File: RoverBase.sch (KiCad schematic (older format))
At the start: 62 parts, among them J1 Conn_01x01, J2 Conn_01x06, J3 Conn_01x04, J4 Conn_01x02, J5 Conn_01x03, J6 Conn_02x03_Counter_Clockwise, J7 Conn_02x03_Counter_Clockwise, J8 Conn_01x01, J9 Conn_01x06, SW1 SW_SPDT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

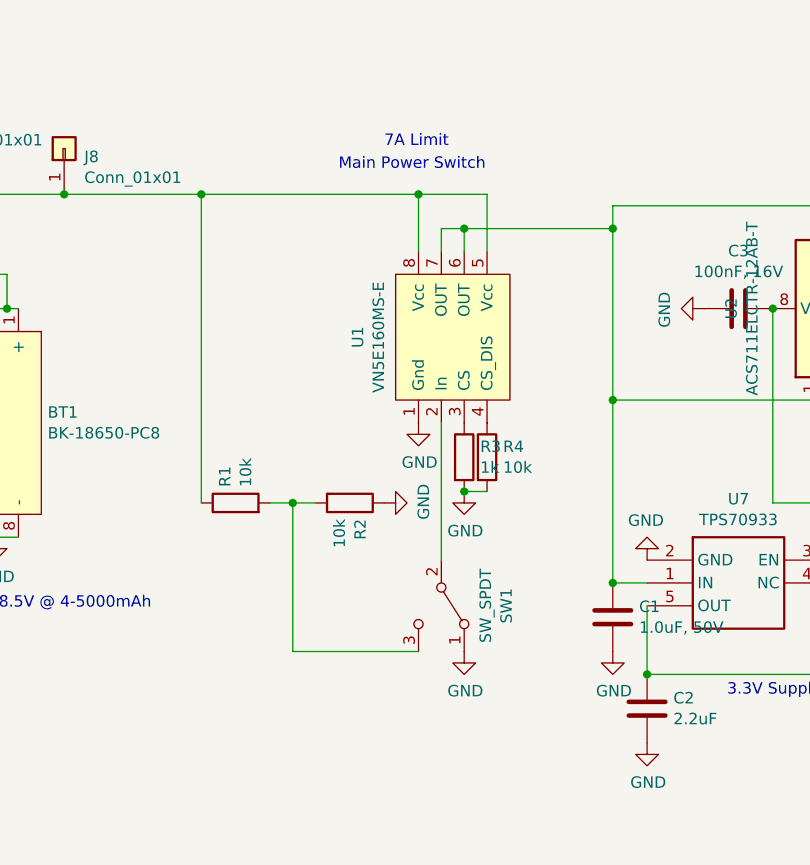
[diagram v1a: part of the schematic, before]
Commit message: Using FET and fuse instead of switch
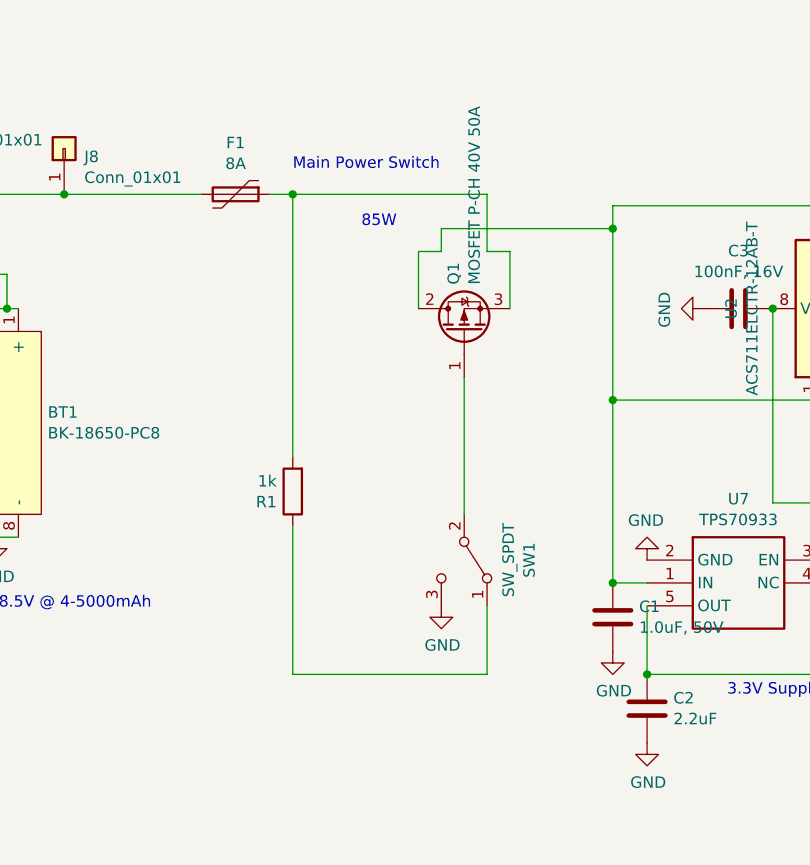
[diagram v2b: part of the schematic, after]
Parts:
- removed R2, R4: 10k, Resistor_SMD:R_0402_1005Metric_Pad0.72x0.64mm_HandSolder, symbol Device:R
- removed R3: 1k, Resistor_SMD:R_0402_1005Metric_Pad0.72x0.64mm_HandSolder, symbol Device:R
- removed U1: VN5E160MS-E, Package_SO:SO-8_3.9x4.9mm_P1.27mm, symbol ST_Switch:VN5E160MS-E
- added F1: 8A, Fuse:Fuse_Bourns_MF-RG800, symbol Device:Polyfuse
- added Q1: MOSFET P-CH 40V 50A, Package_TO_SOT_SMD:TO-263-2, symbol Device:Q_PMOS_GDS
- R1: value 10k -> 1k; MPN CRCW040210K0FKED -> CRCW04021K00FKEDHP; SPN 541-3959-1-ND -> 541-1.00KYCT-ND
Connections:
- net GND: now also SW1.3 (C); no longer SW1.1 (A)
- net at C1.1, R5.1, U2.1 (IP+)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: now also Q1.2 (D)
- net at SW1.2 (B): now also Q1.1 (G)
- net at BT1.3 (+), BT1.4 (+), J8.1 (Pin_1): now also F1.2; no longer R1.1
- net at R1.2: now also F1.1, Q1.3 (S); no longer SW1.3 (C)
- new net: R1.1, SW1.1 (A)
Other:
- note added: "85W"
- note removed: "7A Limit"
- moved on the sheet: SW1
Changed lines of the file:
@@
 Wire Wire Line
 	8450 1750 8350 1750
-Text Notes 3300 1200 0    50   ~ 0
+Text Notes 3100 1200 0    50   ~ 0
 Main Power Switch
 $Comp
@@
 Wire Wire Line
 	4500 1350 4500 1450
-Wire Wire Line
-	3950 1300 3650 1300
-Connection ~ 3650 1300
-Wire Wire Line
-	3650 1300 2700 1300
-Wire Wire Line
-	3750 1450 3850 1450
 Connection ~ 4500 1450
 Wire Wire Line
 	4500 1450 4500 2200
-Connection ~ 3850 1450
 Wire Wire Line
 	3950 1550 3950 1300
 Wire Wire Line
-	3850 1550 3850 1450
-Wire Wire Line
 	3750 1550 3750 1450
-Wire Wire Line
-	3650 1550 3650 1300
-$Comp
-L ST_Switch:VN5E160MS-E U1
-U 1 1 5FB454D3
-P 3550 1950
-F 0 "U1" H 3575 2115 50  0000 C CNN
-F 1 "VN5E160MS-E" H 3575 2024 50  0000 C CNN
-F 2 "Package_SO:SO-8_3.9x4.9mm_P1.27mm" H 3350 1400 50  0001 C CNN
-F 3 "https://www.st.com/content/ccc/resource/technical/document/datasheet/group2/73/be/a4/20/c7/b9/4c/b0/CD00235846/files/CD00235846.pdf/jcr:content/translations/en.CD00235846.pdf" H 3350 1400 50  0001 C CNN
-F 4 "497-11685-1-ND" H 3550 1950 50  0001 C CNN "SPN"
-F 5 "VN5E160MSTR-E" H 3550 1950 50  0001 C CNN "MPN"
-F 6 "STMicroelectronics" H 3550 1950 50  0001 C CNN "Manufacturer"
-	1    3550 1950
-	0    -1   -1   0
-$EndComp
 Text Notes 1150 2500 1    50   ~ 0
 4A max discharge
 $Comp
-L power:GND #PWR04
-U 1 1 5FB52F4F
-P 3650 2300
-F 0 "#PWR04" H 3650 2050 50  0001 C CNN
-F 1 "GND" H 3655 2127 50  0000 C CNN
-F 2 "" H 3650 2300 50  0001 C CNN
-F 3 "" H 3650 2300 50  0001 C CNN
-	1    3650 2300
-	1    0    0    -1
-$EndComp
-$Comp
-L Device:R R3
-U 1 1 5FB5349F
-P 3850 2450
-F 0 "R3" H 3920 2496 50  0000 L CNN
-F 1 "1k" H 3920 2405 50  0000 L CNN
-F 2 "Resistor_SMD:R_0402_1005Metric_Pad0.72x0.64mm_HandSolder" V 3780 2450 50  0001 C CNN
-F 3 "~" H 3850 2450 50  0001 C CNN
-F 4 "CRCW04021K00FKEDHP" H 3850 2450 50  0001 C CNN "MPN"
-F 5 "541-1.00KYCT-ND" H 3850 2450 50  0001 C CNN "SPN"
-F 6 "Vishay Dale" H 3850 2450 50  0001 C CNN "Manufacturer"
-	1    3850 2450
-	1    0    0    -1
-$EndComp
-$Comp
-L Device:R R4
-U 1 1 5FB53A58
-P 3950 2450
-F 0 "R4" H 4020 2496 50  0000 L CNN
-F 1 "10k" H 4020 2405 50  0000 L CNN
-F 2 "Resistor_SMD:R_0402_1005Metric_Pad0.72x0.64mm_HandSolder" V 3880 2450 50  0001 C CNN
-F 3 "~" H 3950 2450 50  0001 C CNN
-F 4 "CRCW040210K0FKED" H 3950 2450 50  0001 C CNN "MPN"
-F 5 "541-3959-1-ND" H 3950 2450 50  0001 C CNN "SPN"
-F 6 "Vishay Dale" H 3950 2450 50  0001 C CNN "Manufacturer"
-	1    3950 2450
-	1    0    0    -1
-$EndComp
-$Comp
-L Device:R R1
-U 1 1 5FB5423C
-P 2850 2650
-F 0 "R1" H 2920 2696 50  0000 L CNN
-F 1 "10k" H 2920 2605 50  0000 L CNN
-F 2 "Resistor_SMD:R_0402_1005Metric_Pad0.72x0.64mm_HandSolder" V 2780 2650 50  0001 C CNN
-F 3 "~" H 2850 2650 50  0001 C CNN
-F 4 "CRCW040210K0FKED" H 2850 2650 50  0001 C CNN "MPN"
-F 5 "541-3959-1-ND" H 2850 2650 50  0001 C CNN "SPN"
-F 6 "Vishay Dale" H 2850 2650 50  0001 C CNN "Manufacturer"
-	1    2850 2650
-	0    -1   -1   0
-$EndComp
-$Comp
-L Device:R R2
-U 1 1 5FB547F5
-P 3350 2650
-F 0 "R2" H 3420 2696 50  0000 L CNN
-F 1 "10k" H 3420 2605 50  0000 L CNN
-F 2 "Resistor_SMD:R_0402_1005Metric_Pad0.72x0.64mm_HandSolder" V 3280 2650 50  0001 C CNN
-F 3 "~" H 3350 2650 50  0001 C CNN
-F 4 "CRCW040210K0FKED" H 3350 2650 50  0001 C CNN "MPN"
-F 5 "541-3959-1-ND" H 3350 2650 50  0001 C CNN "SPN"
-F 6 "Vishay Dale" H 3350 2650 50  0001 C CNN "Manufacturer"
-	1    3350 2650
-	0    1    1    0
-$EndComp
-Wire Wire Line
-	2700 2650 2700 1300
-Connection ~ 2700 1300
-Wire Wire Line
-	3950 2600 3850 2600
-$Comp
-L power:GND #PWR05
-U 1 1 5FB578B0
-P 3850 2600
-F 0 "#PWR05" H 3850 2350 50  0001 C CNN
-F 1 "GND" H 3855 2427 50  0000 C CNN
-F 2 "" H 3850 2600 50  0001 C CNN
-F 3 "" H 3850 2600 50  0001 C CNN
-	1    3850 2600
-	1    0    0    -1
-$EndComp
-Connection ~ 3850 2600
-$Comp
-L power:GND #PWR03
-U 1 1 5FB57DBB
-P 3500 2650
-F 0 "#PWR03" H 3500 2400 50  0001 C CNN
-F 1 "GND" H 3505 2477 50  0000 C CNN
-F 2 "" H 3500 2650 50  0001 C CNN
-F 3 "" H 3500 2650 50  0001 C CNN
-	1    3500 2650
-	0    -1   -1   0
-$EndComp
-$Comp
 L Switch:SW_SPDT SW1
 U 1 1 5FB5A453
-P 3750 3100
-F 0 "SW1" H 3750 3385 50  0000 C CNN
-F 1 "SW_SPDT" H 3750 3294 50  0000 C CNN
-F 2 "Button_Switch_THT:SW_CuK_OS102011MA1QN1_SPDT_Angled" H 3750 3100 50  0001 C CNN
-F 3 "~" H 3750 3100 50  0001 C CNN
-F 4 "OS102011MA1QN1" H 3750 3100 50  0001 C CNN "MPN"
-F 5 "CKN9559-ND" H 3750 3100 50  0001 C CNN "SPN"
-F 6 "C&K" H 3750 3100 50  0001 C CNN "Manufacturer"
-	1    3750 3100
+P 3850 2900
+F 0 "SW1" H 3850 3185 50  0000 C CNN
+F 1 "SW_SPDT" H 3850 3094 50  0000 C CNN
+F 2 "Button_Switch_THT:SW_CuK_OS102011MA1QN1_SPDT_Angled" H 3850 2900 50  0001 C CNN
+F 3 "~" H 3850 2900 50  0001 C CNN
+F 4 "OS102011MA1QN1" H 3850 2900 50  0001 C CNN "MPN"
+F 5 "CKN9559-ND" H 3850 2900 50  0001 C CNN "SPN"
+F 6 "C&K" H 3850 2900 50  0001 C CNN "Manufacturer"
+	1    3850 2900
 	0    1    1    0
 $EndComp
-Wire Wire Line
-	3750 2300 3750 2900
-Wire Wire Line
-	3650 3300 3100 3300
-Wire Wire Line
-	3100 3300 3100 2650
-Wire Wire Line
-	3100 2650 3000 2650
-Wire Wire Line
-	3200 2650 3100 2650
-Connection ~ 3100 2650
 $Comp
 L power:GND #PWR06
 U 1 1 5FB65CD7
-P 3850 3300
-F 0 "#PWR06" H 3850 3050 50  0001 C CNN
-F 1 "GND" H 3855 3127 50  0000 C CNN
-F 2 "" H 3850 3300 50  0001 C CNN
-F 3 "" H 3850 3300 50  0001 C CNN
-	1    3850 3300
+P 3750 3100
+F 0 "#PWR06" H 3750 2850 50  0001 C CNN
+F 1 "GND" H 3755 2927 50  0000 C CNN
+F 2 "" H 3750 3100 50  0001 C CNN
+F 3 "" H 3750 3100 50  0001 C CNN
+	1    3750 3100
 	1    0    0    -1
 $EndComp
@@
 	0    1    1    0
 $EndComp
-Text Notes 3500 1100 0    50   ~ 0
-7A Limit
+Text Notes 3400 1450 0    50   ~ 0
+85W
 Wire Wire Line
 	7100 4900 7200 4900
@@
 $EndComp
 Wire Wire Line
-	3850 1450 4500 1450
-Wire Wire Line
 	7200 4900 8200 4900
 $Comp
@@
 Connection ~ 2100 1300
 Wire Wire Line
-	2100 1300 2700 1300
-Wire Wire Line
 	1450 1300 2100 1300
 $Comp
@@
 	9350 4900 9050 4900
 Connection ~ 9350 4900
+$Comp
+L Device:Q_PMOS_GDS Q1
+U 1 1 60C92188
+P 3850 1900
+F 0 "Q1" H 4055 1946 50  0000 L CNN
+F 1 " MOSFET P-CH 40V 50A" H 4055 1855 50  0000 L CNN
+F 2 "Package_TO_SOT_SMD:TO-263-2" H 4050 2000 50  0001 C CNN
+F 3 "~" H 3850 1900 50  0001 C CNN
+F 4 "SQM40081EL_GE3" H 3850 1900 50  0001 C CNN "MPN"
+F 5 "Vishay Siliconix" H 3850 1900 50  0001 C CNN "Manufacturer"
+F 6 "SQM40081EL_GE3CT-ND" H 3850 1900 50  0001 C CNN "SPN"
+	1    3850 1900
+	0    -1   -1   0
+$EndComp
+Wire Wire Line
+	3750 1450 4500 1450
+Wire Wire Line
+	3950 3100 3950 3400
+Wire Wire Line
+	3950 3400 3100 3400
+$Comp
+L Device:R R1
+U 1 1 60CD74FE
+P 3100 2600
+F 0 "R1" H 3170 2646 50  0000 L CNN
+F 1 "1k" H 3170 2555 50  0000 L CNN
+F 2 "Resistor_SMD:R_0402_1005Metric_Pad0.72x0.64mm_HandSolder" V 3030 2600 50  0001 C CNN
+F 3 "~" H 3100 2600 50  0001 C CNN
+F 4 "CRCW04021K00FKEDHP" H 3100 2600 50  0001 C CNN "MPN"
+F 5 "541-1.00KYCT-ND" H 3100 2600 50  0001 C CNN "SPN"
+F 6 "Vishay Dale" H 3100 2600 50  0001 C CNN "Manufacturer"
+	1    3100 2600
+	-1   0    0    1
+$EndComp
+Connection ~ 3100 1300
+Wire Wire Line
+	3100 1300 3950 1300
+Wire Wire Line
+	3100 1300 3100 2450
+Wire Wire Line
+	2100 1300 2700 1300
+Wire Wire Line
+	3650 1800 3650 1550
+Wire Wire Line
+	3650 1550 3750 1550
+Wire Wire Line
+	4050 1800 4050 1550
+Wire Wire Line
+	4050 1550 3950 1550
+Wire Wire Line
+	3100 2750 3100 3400
+Wire Wire Line
+	3850 2100 3850 2700
+$Comp
+L Device:Polyfuse F1
+U 1 1 60CF1E6D
+P 2850 1300
+F 0 "F1" V 2625 1300 50  0000 C CNN
+F 1 "8A" V 2716 1300 50  0000 C CNN
+F 2 "Fuse:Fuse_Bourns_MF-RG800" H 2900 1100 50  0001 L CNN
+F 3 "~" H 2850 1300 50  0001 C CNN
+F 4 " Bourns Inc. " H 2850 1300 50  0001 C CNN "MPN"
+F 5 " MF-RG800-2 " H 2850 1300 50  0001 C CNN "Manufacturer"
+F 6 "118-MF-RG800-2CT-ND" H 2850 1300 50  0001 C CNN "SPN"
+	1    2850 1300
+	0    1    1    0
+$EndComp
+Wire Wire Line
+	3000 1300 3100 1300
 $EndSCHEMATC
